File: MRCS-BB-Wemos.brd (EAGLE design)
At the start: 81.3 x 50.8 mm, 11 parts, among them IC1 MCP23017SP

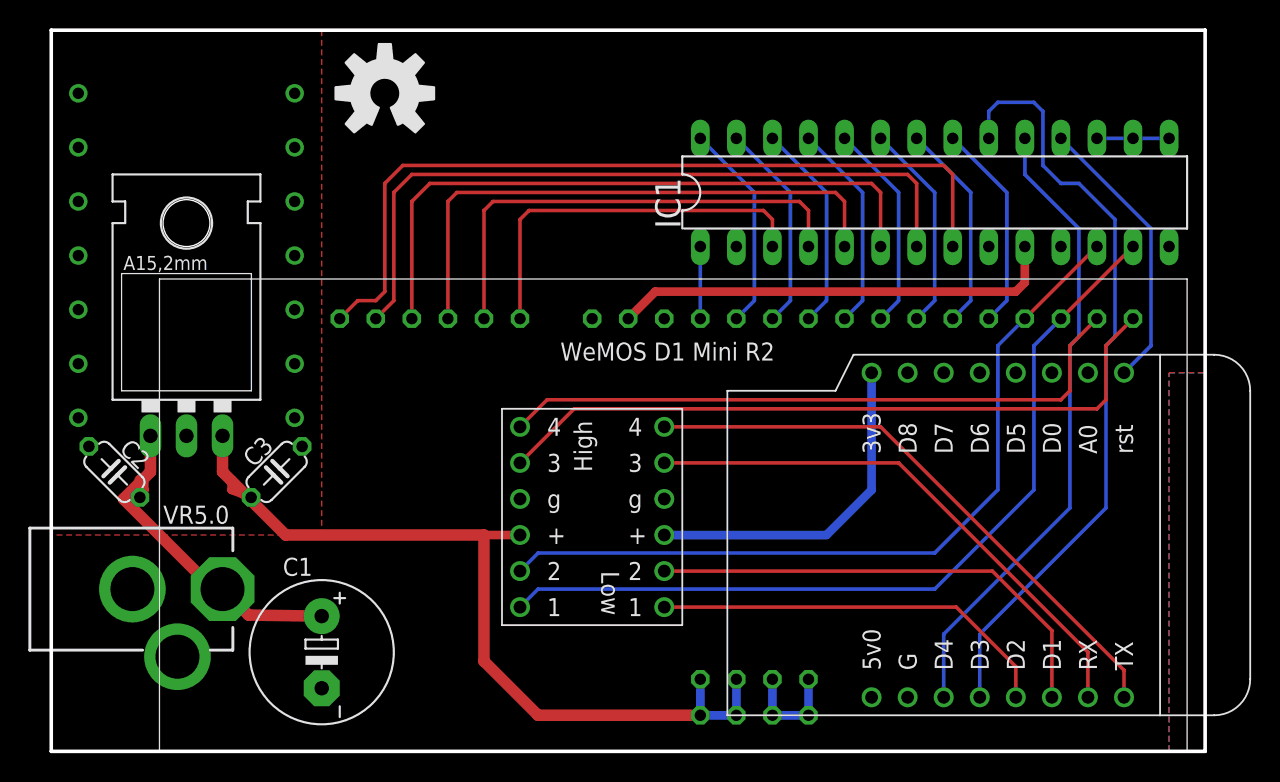
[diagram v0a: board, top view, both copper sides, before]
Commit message: replace / update components with newer ones in SPCoast library clean up silk screen, add MRCS
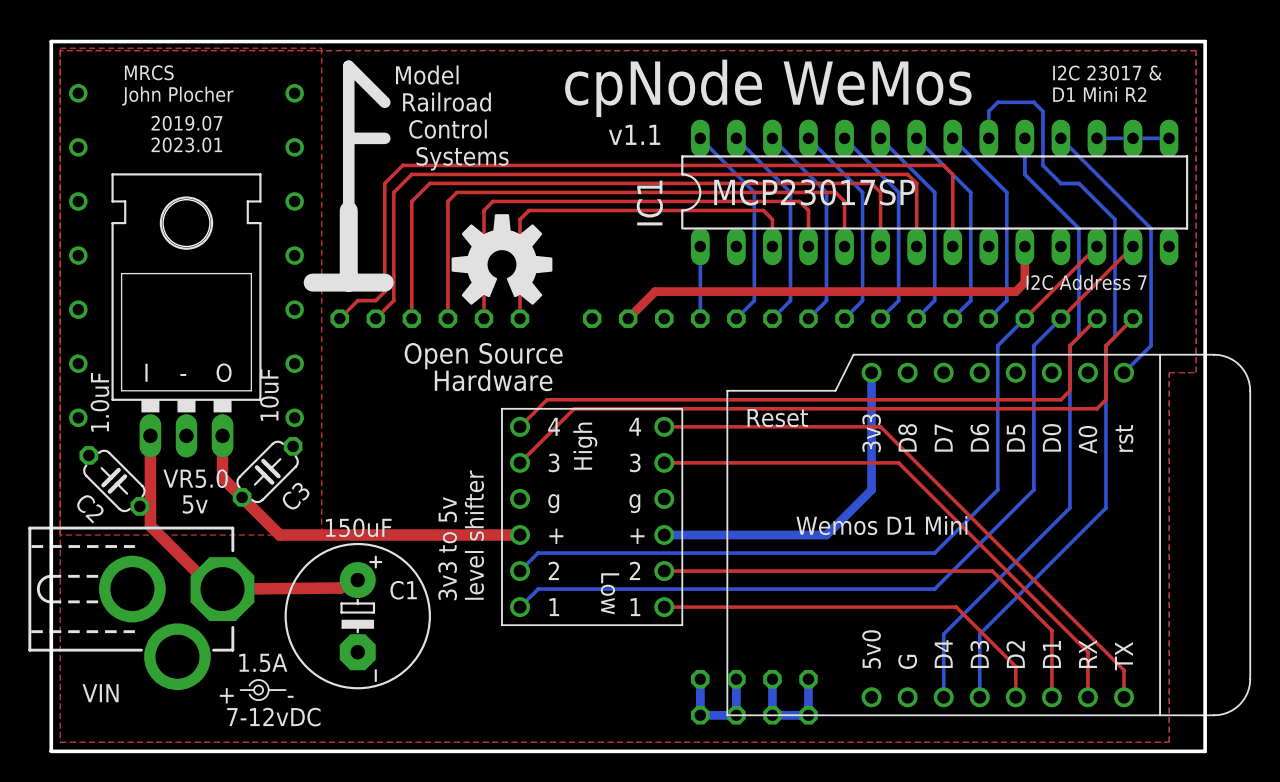
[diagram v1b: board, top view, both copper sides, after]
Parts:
- added U$1: DOC-MRCS-LOGOTOP, SPCoast:MRCS-LOGO
- C1: device SPCoast:E5-10,5 -> SPCoast:E5-10.5
- IC1: device microchip:DIL28-3 -> SPCoast:DIL28-3
- LABEL1: device SPCoast-minimal:POWER_USAGE -> SPCoast:PWR_LABEL
- OSHW1: value OSHW-LOGOL -> DOC-OSHW-LOGO-L; device SparkFun:OSHW-LOGO-L -> SPCoast:OSHW-LOGO-L
- moved OSHW1 14.6 mm to (31.8, 34.3)
- moved LABEL1 9.54 mm to (14.6, 4.32)
- moved C1 3.59 mm to (21.6, 9.53)
- moved C3 0.63 mm to (15.2, 19.7)
- moved C2 0.63 mm to (4.45, 19.1)
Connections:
- net SCLH: now also BBLEO.SCL; no longer BBLEO.D3
- net SDAH: now also BBLEO.SDA; no longer BBLEO.D2
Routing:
- net VCCIO: track 67.8 -> 38.3 mm
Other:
- board size 81.3 x 50.8 mm -> 81.3 x 50 mm
- board text added: "1.0uF"
- board text added: "10uF"
- board text added: "150uF"
- board text added: "2019.07 2023.01"
- board text added: "3v3 to 5v level shifter"
- board text added: "5v"
- board text added: "C1"
- board text added: "C2"
- board text added: "C3"
- board text added: "D1 Mini"
- board text added: "I2C 23017 & D1 Mini R2"
- board text added: "IC1"
- board text added: "MCP23017SP"
- board text added: "MRCS John Plocher"
- board text added: "VR5.0"
- board text added: "Wemos D1 Mini"
- board text added: "cpNode Wemos"
- board text added: "v1.1"
- board text removed: "2019.07"
- board text removed: "John Plocher"
- board text removed: "WeMOS D1 Mini R2"
- board text removed: "cpNode WeMOS D1 Mini"
- board text removed: "v1.0"

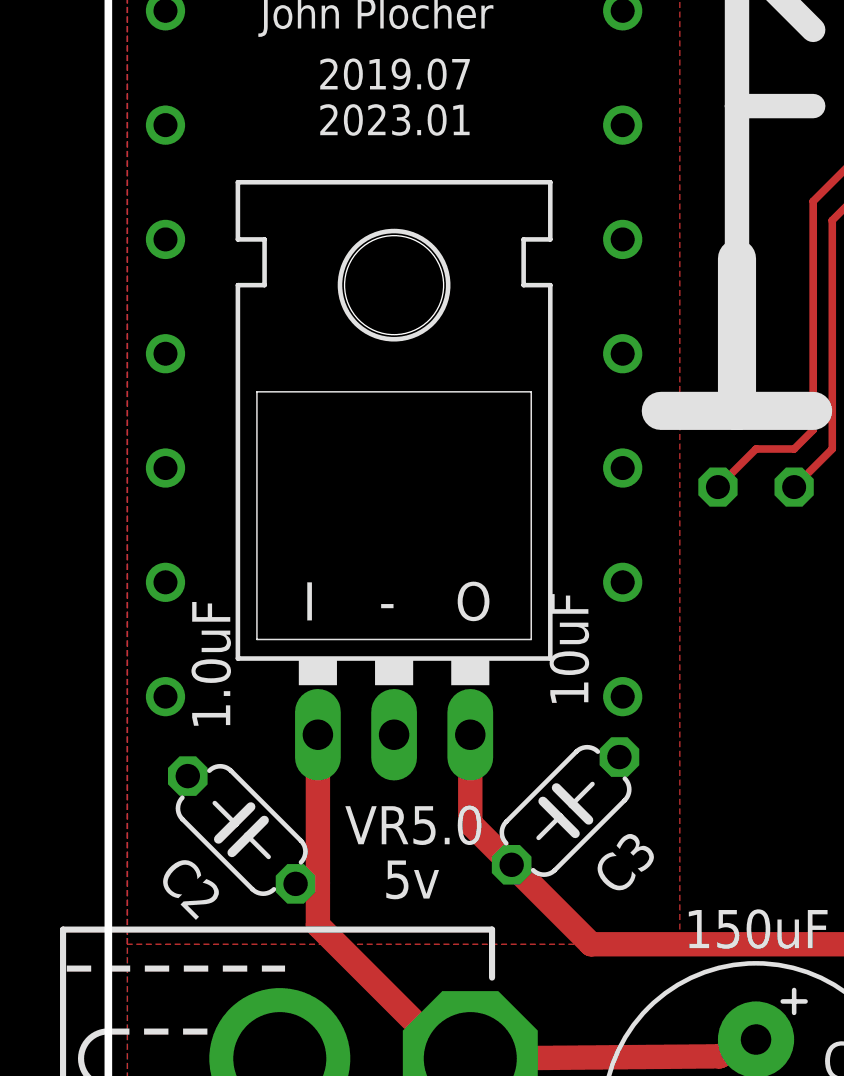
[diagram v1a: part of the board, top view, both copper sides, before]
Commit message: replace VR with RA version & mounting hole to W/A an eagle bug Add MRCS to sch
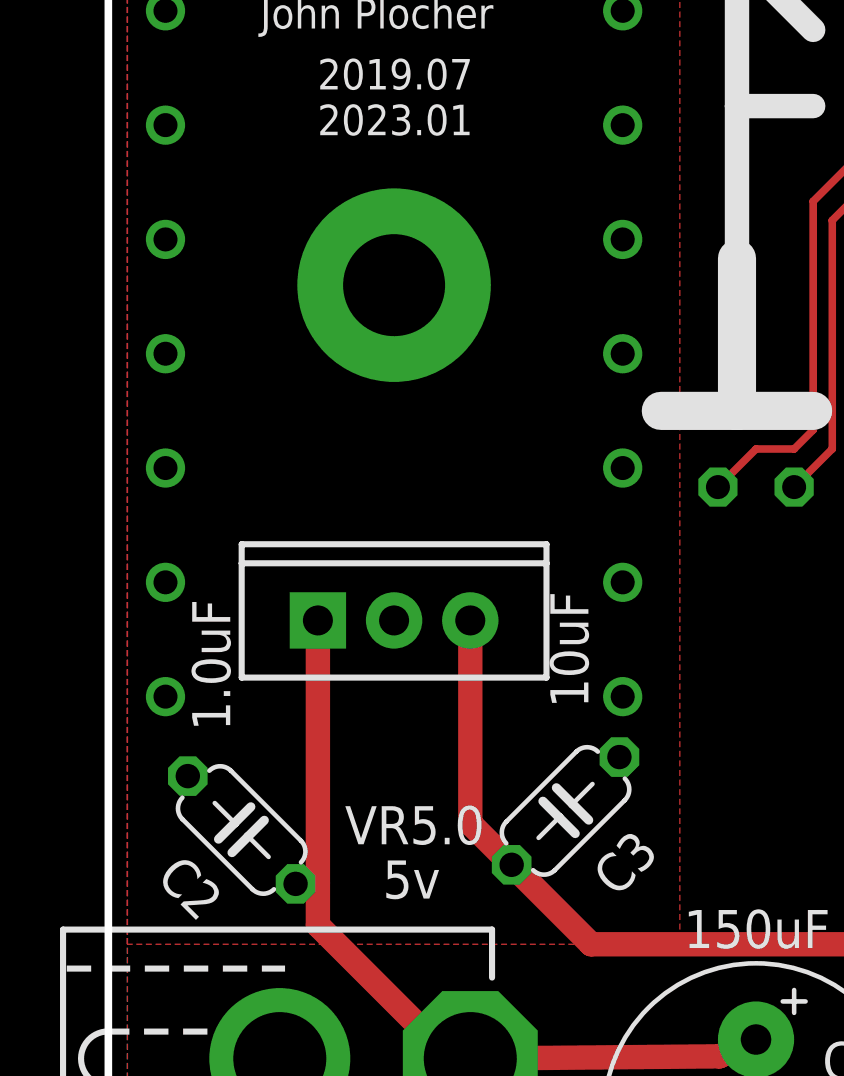
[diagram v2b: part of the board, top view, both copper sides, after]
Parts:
- VR5.0: device SPCoast:TO-220 -> SPCoast:TO-220-RA
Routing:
- net +9V: track 23.7 -> 27.5 mm
- net VCCIO: track 38.3 -> 42.1 mm
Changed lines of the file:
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@@
 <setting verticaltext="up"/>
 </settings>
-<grid distance="50" unitdist="mil" unit="mil" style="dots" multiple="2" display="yes" altdistance="25" altunitdist="mil" altunit="mil"/>
+<grid distance="50" unitdist="mil" unit="mm" style="dots" multiple="2" display="yes" altdistance="5" altunitdist="mil" altunit="mm"/>
 <layers>
 <layer number="1" name="Top" color="4" fill="1" visible="yes" active="yes"/>
@@
 <layer number="98" name="Guide" color="6" fill="1" visible="no" active="no"/>
 <layer number="99" name="Anatomie" color="7" fill="1" visible="no" active="no"/>
+<layer number="100" name="Muster" color="7" fill="1" visible="no" active="no"/>
+<layer number="101" name="Hidden" color="57" fill="4" visible="yes" active="yes"/>
+<layer number="102" name="Changes" color="13" fill="1" visible="yes" active="yes"/>
+<layer number="103" name="tMap" color="29" fill="4" visible="yes" active="yes"/>
+<layer number="104" name="Name" color="16" fill="1" visible="yes" active="yes"/>
+<layer number="105" name="tPlate" color="7" fill="1" visible="yes" active="yes"/>
+<layer number="106" name="bPlate" color="7" fill="1" visible="yes" active="yes"/>
+<layer number="107" name="Crop" color="7" fill="1" visible="yes" active="yes"/>
+<layer number="108" name="fp8" color="7" fill="1" visible="yes" active="yes"/>
+<layer number="109" name="fp9" color="7" fill="1" visible="yes" active="yes"/>
+<layer number="110" name="fp0" color="7" fill="1" visible="yes" active="yes"/>
+<layer number="111" name="bdokum" color="7" fill="1" visible="yes" active="yes"/>
+<layer number="112" name="tSilk" color="7" fill="1" visible="no" active="no"/>
+<layer number="113" name="IDFDebug" color="7" fill="1" visible="yes" active="yes"/>
+<layer number="114" name="Rect_Pads" color="7" fill="1" visible="yes" active="yes"/>
+<layer number="115" name="_tsilk" color="7" fill="1" visible="yes" active="yes"/>
+<layer number="116" name="Patch_BOT" color="9" fill="4" visible="yes" active="yes"/>
+<layer number="117" name="tTestmark" color="7" fill="1" visible="yes" active="yes"/>
+<layer number="118" name="Rect_Pads" color="7" fill="1" visible="no" active="no"/>
+<layer number="119" name="_tNames" color="7" fill="1" visible="yes" active="yes"/>
+<layer number="120" name="_bNames" color="7" fill="1" visible="yes" active="yes"/>
+<layer number="121" name="_tsilk" color="7" fill="1" visible="yes" active="yes"/>
+<layer number="122" name="_bsilk" color="7" fill="1" visible="yes" active="yes"/>
+<layer number="123" name="tTestmark" color="7" fill="1" visible="yes" active="yes"/>
+<layer number="124" name="bTestmark" color="7" fill="1" visible="yes" active="yes"/>
 <layer number="125" name="_tNames" color="14" fill="1" visible="no" active="yes"/>
+<layer number="126" name="_bNames" color="7" fill="1" visible="yes" active="yes"/>
+<layer number="127" name="_tValues" color="7" fill="1" visible="no" active="no"/>
+<layer number="128" name="_bValues" color="7" fill="1" visible="no" active="no"/>
+<layer number="129" name="Mask" color="7" fill="1" visible="yes" active="yes"/>
+<layer number="130" name="SMDSTROOK" color="7" fill="1" visible="yes" active="yes"/>
+<layer number="131" name="tAdjust" color="7" fill="1" visible="yes" active="yes"/>
+<layer number="132" name="bAdjust" color="7" fill="1" visible="yes" active="yes"/>
+<layer number="144" name="Drill_legend" color="7" fill="1" visible="yes" active="yes"/>
+<layer number="146" name="Housing" color="7" fill="1" visible="yes" active="yes"/>
+<layer number="147" name="Edge" color="7" fill="1" visible="yes" active="yes"/>
+<layer number="148" name="ReferenceLC" color="7" fill="1" visible="yes" active="yes"/>
+<layer number="149" name="ReferenceLS" color="7" fill="1" visible="yes" active="yes"/>
+<layer number="150" name="Notes" color="7" fill="1" visible="yes" active="yes"/>
+<layer number="151" name="HeatSink" color="7" fill="1" visible="yes" active="yes"/>
+<layer number="152" name="_bDocu" color="7" fill="1" visible="no" active="no"/>
+<layer number="153" name="FabDoc1" color="7" fill="1" visible="yes" active="yes"/>
+<layer number="154" name="FabDoc2" color="7" fill="1" visible="yes" active="yes"/>
+<layer number="155" name="FabDoc3" color="7" fill="1" visible="yes" active="yes"/>
+<layer number="199" name="Contour" color="7" fill="1" visible="yes" active="yes"/>
+<layer number="200" name="200bmp" color="1" fill="10" visible="yes" active="yes"/>
+<layer number="201" name="201bmp" color="2" fill="10" visible="yes" active="yes"/>
+<layer number="202" name="202bmp" color="3" fill="10" visible="yes" active="yes"/>
+<layer number="203" name="203bmp" color="4" fill="10" visible="yes" active="yes"/>
+<layer number="204" name="204bmp" color="5" fill="10" visible="yes" active="yes"/>
+<layer number="205" name="205bmp" color="6" fill="10" visible="yes" active="yes"/>
+<layer number="206" name="206bmp" color="7" fill="10" visible="yes" active="yes"/>
+<layer number="207" name="207bmp" color="8" fill="10" visible="yes" active="yes"/>
+<layer number="208" name="208bmp" color="9" fill="10" visible="yes" active="yes"/>
+<layer number="209" name="209bmp" color="7" fill="1" visible="yes" active="yes"/>
+<layer number="210" name="210bmp" color="7" fill="1" visible="yes" active="yes"/>
+<layer number="211" name="211bmp" color="12" fill="1" visible="no" active="no"/>
+<layer number="212" name="212bmp" color="13" fill="1" visible="no" active="no"/>
+<layer number="213" name="213bmp" color="14" fill="1" visible="no" active="no"/>
+<layer number="214" name="214bmp" color="15" fill="1" visible="no" active="no"/>
+<layer number="215" name="215bmp" color="16" fill="1" visible="no" active="no"/>
+<layer number="216" name="216bmp" color="17" fill="1" visible="no" active="no"/>
+<layer number="217" name="217bmp" color="18" fill="1" visible="no" active="no"/>
+<layer number="218" name="218bmp" color="19" fill="1" visible="no" active="no"/>
+<layer number="219" name="219bmp" color="20" fill="1" visible="no" active="no"/>
+<layer number="220" name="220bmp" color="21" fill="1" visible="no" active="no"/>
+<layer number="221" name="221bmp" color="22" fill="1" visible="no" active="no"/>
+<layer number="222" name="222bmp" color="23" fill="1" visible="no" active="no"/>
+<layer number="223" name="223bmp" color="24" fill="1" visible="no" active="no"/>
+<layer number="224" name="224bmp" color="25" fill="1" visible="no" active="no"/>
+<layer number="225" name="225bmp" color="7" fill="1" visible="yes" active="yes"/>
+<layer number="226" name="226bmp" color="7" fill="1" visible="yes" active="yes"/>
+<layer number="227" name="227bmp" color="7" fill="1" visible="yes" active="yes"/>
+<layer number="228" name="228bmp" color="7" fill="1" visible="yes" active="yes"/>
+<layer number="229" name="229bmp" color="7" fill="1" visible="yes" active="yes"/>
+<layer number="230" name="230bmp" color="7" fill="1" visible="yes" active="yes"/>
+<layer number="231" name="231bmp" color="7" fill="1" visible="yes" active="yes"/>
+<layer number="232" name="Eagle3D_PG2" color="7" fill="1" visible="yes" active="yes"/>
+<layer number="233" name="Eagle3D_PG3" color="7" fill="1" visible="yes" active="yes"/>
+<layer number="247" name="wrappinf" color="7" fill="1" visible="yes" active="yes"/>
+<layer number="248" name="Housing" color="7" fill="1" visible="no" active="no"/>
+<layer number="249" name="Edge" color="7" fill="1" visible="no" active="no"/>
+<layer number="250" name="Descript" color="3" fill="1" visible="no" active="no"/>
+<layer number="251" name="SMDround" color="12" fill="11" visible="no" active="no"/>
+<layer number="252" name="BR-BS" color="7" fill="1" visible="yes" active="yes"/>
+<layer number="253" name="BR-LS" color="7" fill="1" visible="yes" active="yes"/>
+<layer number="254" name="cooling" color="7" fill="1" visible="yes" active="yes"/>
+<layer number="255" name="routoute" color="7" fill="1" visible="yes" active="yes"/>
 </layers>
 <board>
@@
 <attribute name="VALUE" x="4.064" y="22.352" size="1.27" layer="27" font="vector" rot="R90"/>
 </element>
-<element name="VR5.0" library="SPCoast" package="TO-220" value="5v" x="9.525" y="26.035" smashed="yes">
+<element name="VR5.0" library="SPCoast" package="TO-220-RA" value="5v" x="9.525" y="26.035" smashed="yes">
 <attribute name="NAME" x="12.54125" y="19.84375" size="1.27" layer="25" font="vector" ratio="11" rot="R180"/>
 <attribute name="VALUE" x="9.144" y="16.764" size="1.27" layer="27" font="vector" ratio="10"/>
@@
 <contactref element="VR5.0" pad="IN"/>
 <contactref element="C1" pad="+"/>
-<wire x1="6.985" y1="22.225" x2="6.985" y2="17.272" width="0.8128" layer="1"/>
+<wire x1="6.985" y1="26.035" x2="6.985" y2="17.272" width="0.8128" layer="1"/>
 <wire x1="6.985" y1="17.272" x2="6.985" y2="15.875" width="0.8128" layer="1"/>
 <wire x1="6.24105" y1="17.253946875" x2="6.985" y2="17.272" width="0.8128" layer="1"/>
@@
 <wire x1="48.26" y1="2.54" x2="48.26" y2="5.08" width="0.6096" layer="16"/>
 <contactref element="LS2" pad="HV"/>
-<wire x1="12.065" y1="22.225" x2="12.065" y2="19.26789375" width="0.8128" layer="1"/>
+<wire x1="12.065" y1="26.035" x2="12.065" y2="19.26789375" width="0.8128" layer="1"/>
 <wire x1="12.065" y1="19.26789375" x2="13.443946875" y2="17.888946875" width="0.8128" layer="1"/>
 <wire x1="13.443946875" y1="17.888946875" x2="16.09289375" y2="15.24" width="0.8128" layer="1"/>
@@
 <wire x1="77.47" y1="28.575" x2="75.565" y2="26.67" width="0.254" layer="16"/>
 </signal>
+<signal name="N$1">
+<via x="9.525" y="37.211" extent="1-16" drill="3.4" diameter="6.4516"/>
+</signal>
 </signals>
